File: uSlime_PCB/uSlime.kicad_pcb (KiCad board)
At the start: 2 copper layers, 25 x 22.6 mm, 43 parts, among them CN1 X1502WR-05K-N0SN, CN2 1.25T-2AW, J1 USB_C_Receptacle_USB2.0_14P, U1 ESP32-C6-MINI-1, U2 MSK-12C02_SMD_SPDT_SWITCH, U3 AP2112K-3.3TRG1, U4 MCP73831T-2ACI/OT, U5 BNO085

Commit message: v0.0.4a
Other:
- board text added: "v0.0.4a"
- board text removed: "v0.0.3a"
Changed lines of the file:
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@@
 		(tags "solder jumper open")
 		(property "Reference" "JP1"
-			(at 0 1.8 360)
+			(at 0 1.8 0)
 			(layer "B.SilkS")
 			(hide yes)
@@
 		)
 		(property "Value" "Jumper_3_Open"
-			(at 0 -1.9 360)
+			(at 0 -1.9 0)
 			(layer "B.Fab")
 			(effects
@@
 		)
 	)
-	(gr_text "v0.0.3a"
+	(gr_text "v0.0.4a"
 		(at 113.55 91.25 0)
 		(layer "B.SilkS")

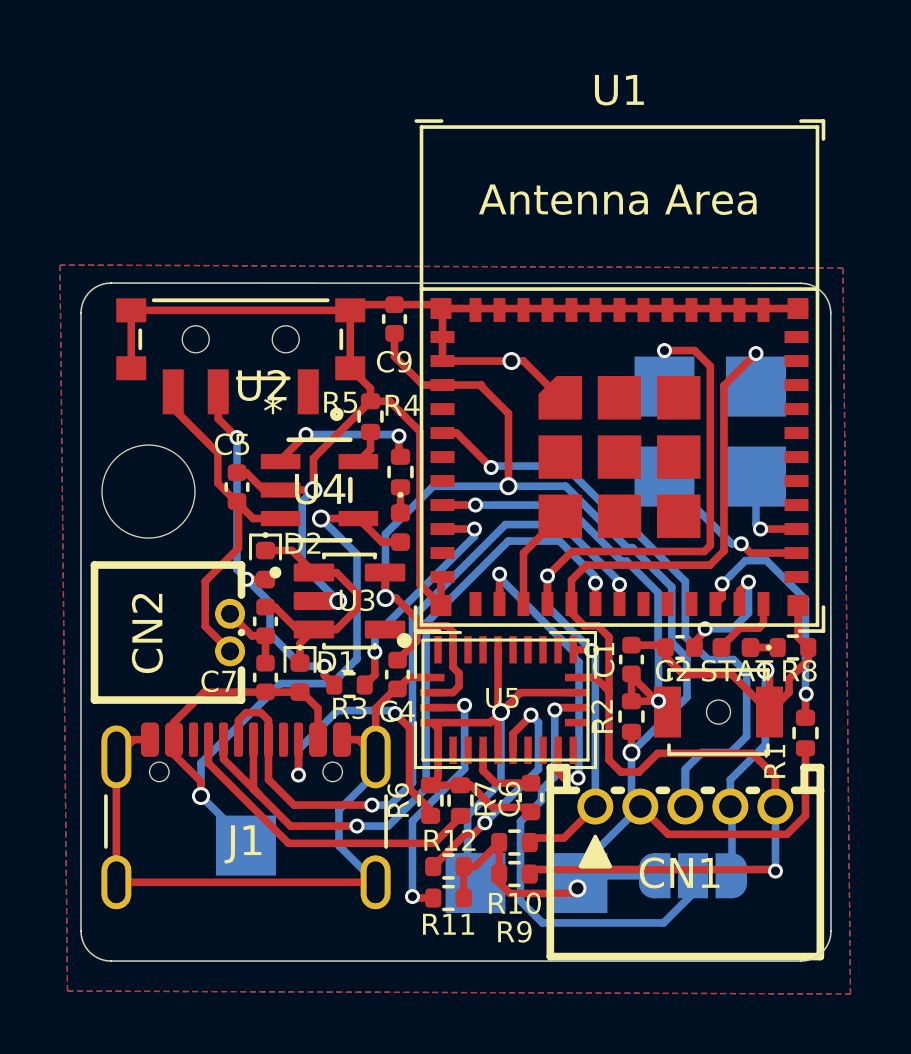
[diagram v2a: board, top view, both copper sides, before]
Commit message: v0.0.5: Invert CLKSEL pin to 3.3V
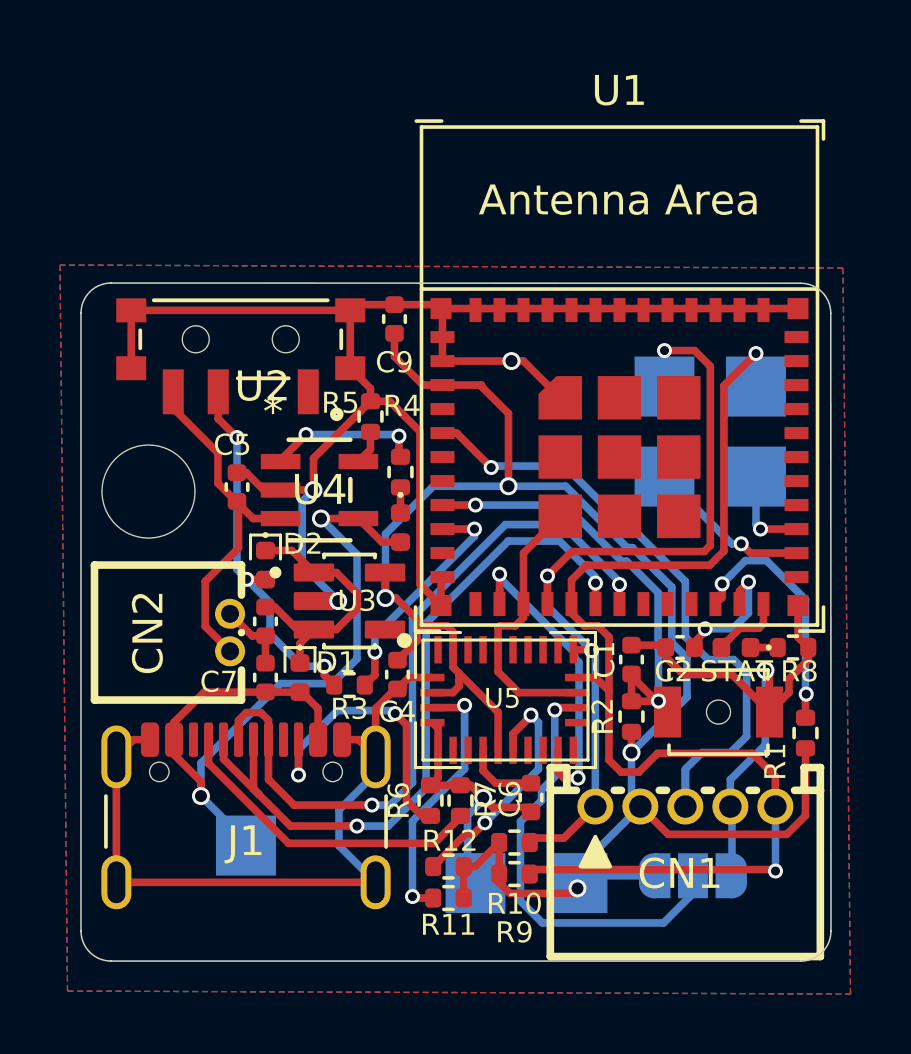
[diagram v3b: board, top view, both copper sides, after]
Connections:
- U5 pad 10: GND -> +3.3V
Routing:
- net GND: track 124.8 -> 118.8 mm
- net +3.3V: track 60.2 -> 63.3 mm
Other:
- board text added: "v0.0.5a"
- board text removed: "v0.0.4a"

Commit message: Connect pin 26 to GND
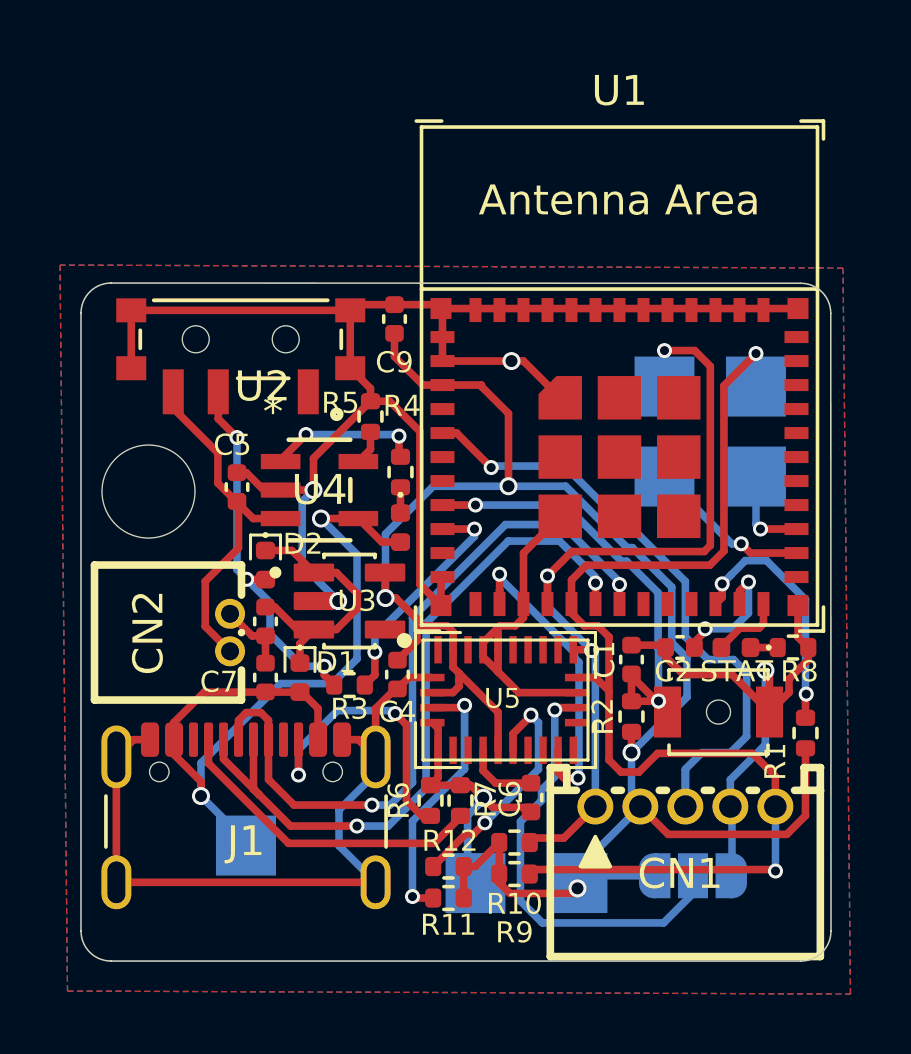
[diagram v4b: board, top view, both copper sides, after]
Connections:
- U5 pad 26: unconnected-(U5-XOUT32/CLKSEL1-Pad26) -> GND
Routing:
- net GND: track 118.8 -> 120.7 mm

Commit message: Add dingyifei to PCB ref
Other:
- board text added: "dingyifei"

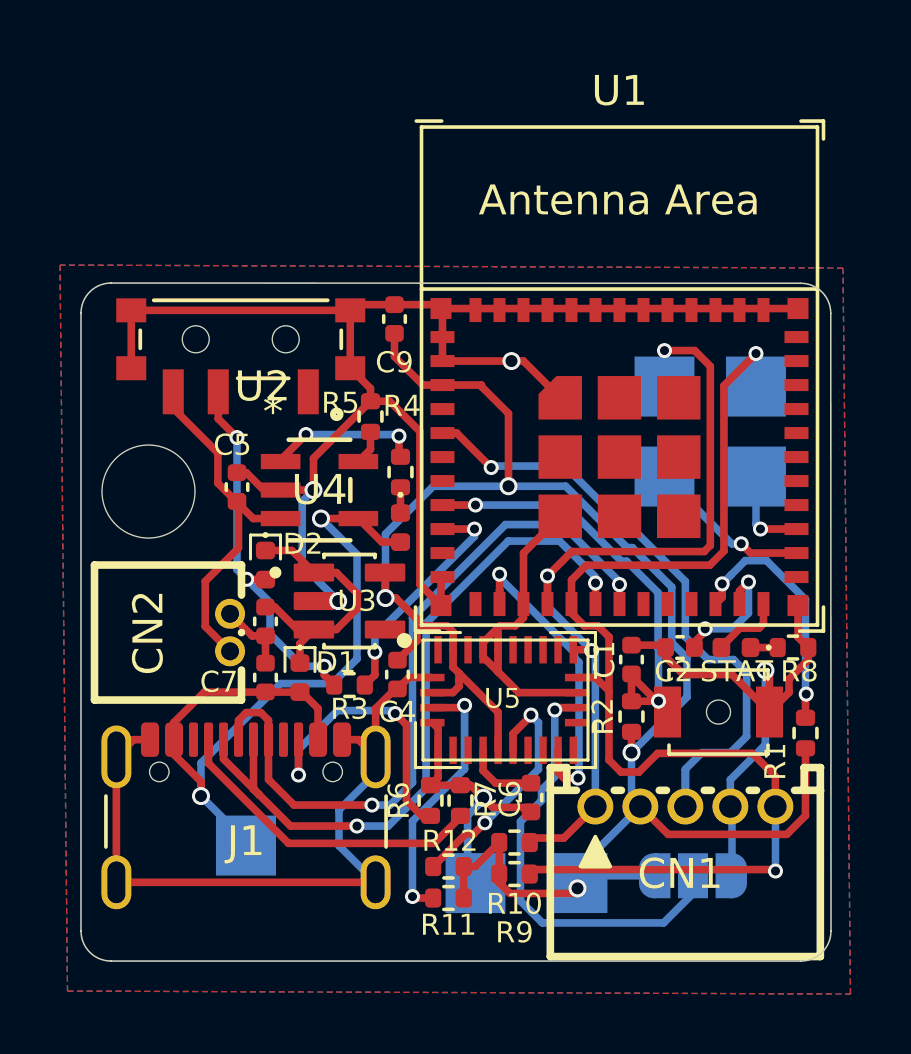
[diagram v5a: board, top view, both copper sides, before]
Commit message: Modify PCB to add resistors to pins 14, 15, 16
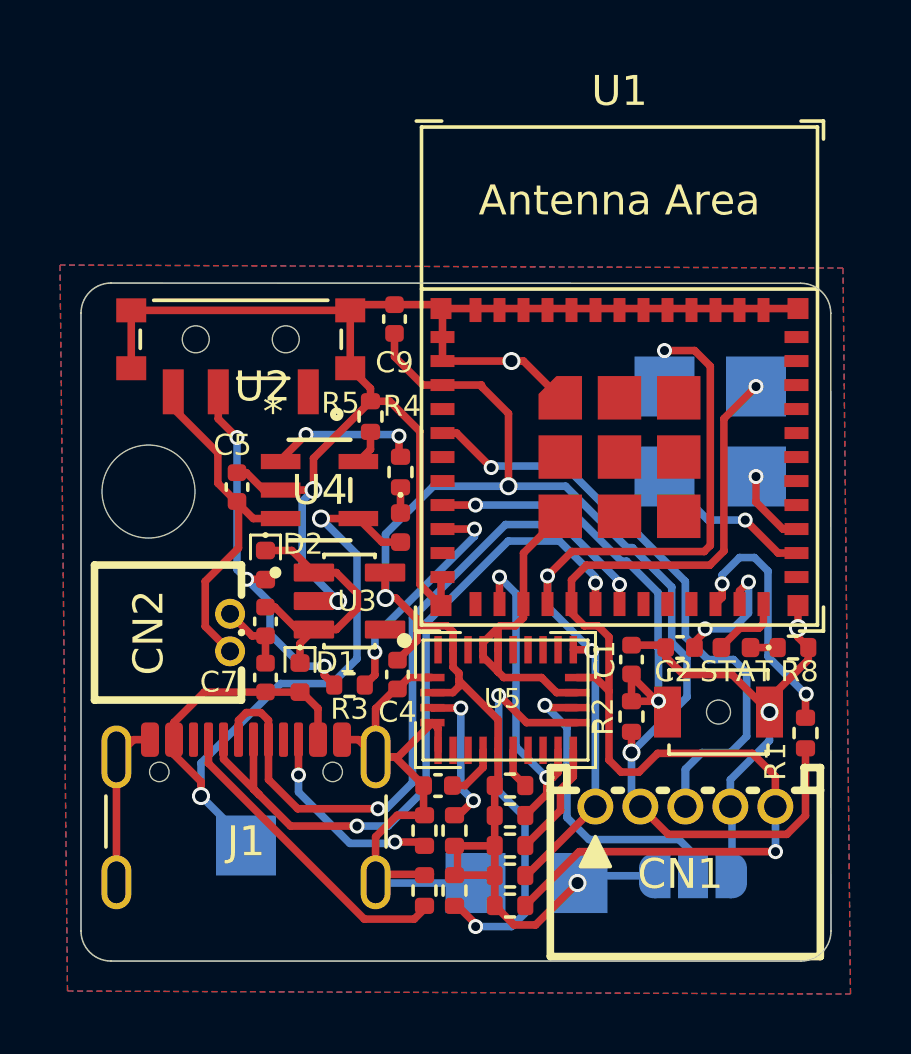
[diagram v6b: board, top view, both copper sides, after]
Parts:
- added R13: 10k, Resistor_SMD:R_0402_1005Metric, F.Cu at (115.0, 107.1)
- added R14: 10k, Resistor_SMD:R_0402_1005Metric, F.Cu at (115.0, 108.1)
- added R15: 10k, Resistor_SMD:R_0402_1005Metric, F.Cu at (113.1, 109.6)
- moved R12 3.39 mm to (115.0, 106.1), turned to 180 degrees
- moved R7 3.23 mm to (112.1, 109.6)
- moved C6 3.13 mm to (112.5, 106.1), turned to 0 degrees
- moved R11 2.26 mm to (113.1, 107.6), turned to 90 degrees
- moved R10 1.11 mm to (115.0, 109.1)
- moved R9 1.06 mm to (115.0, 110.1)
- moved R6 1.02 mm to (112.1, 107.6)
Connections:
- U5 pad 15: unconnected-(U5-ENV_SCL-Pad15) -> Net-(U5-ENV_SCL)
- U5 pad 16: unconnected-(U5-ENV_SDA-Pad16) -> Net-(U5-ENV_SDA)
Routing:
- net Net-(U5-ENV_SDA): track 0.00 -> 13.4 mm, vias 0 -> 2
- net GND: track 120.7 -> 110.1 mm
- net Net-(U5-NRST): track 8.18 -> 1.34 mm, vias 2 -> 0
- net Net-(JP1-C): track 14.7 -> 10.6 mm
- net Net-(U5-BOOTN): track 8.91 -> 4.95 mm
- net Net-(U5-ENV_SCL): track 0.00 -> 3.84 mm
- net Net-(J1-CC2): track 9.90 -> 6.83 mm
- net BNO_SCL: track 39.3 -> 37.3 mm
- net +3.3V: track 63.3 -> 65.0 mm
- net Net-(U5-CAP): track 2.47 -> 1.74 mm
- net BNO_SDA: track 27.3 -> 28.0 mm
- net BNO_INT: track 10.4 -> 11.0 mm

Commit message: v1.0.0 - Use 1206 LED, add resistor pack suggestion
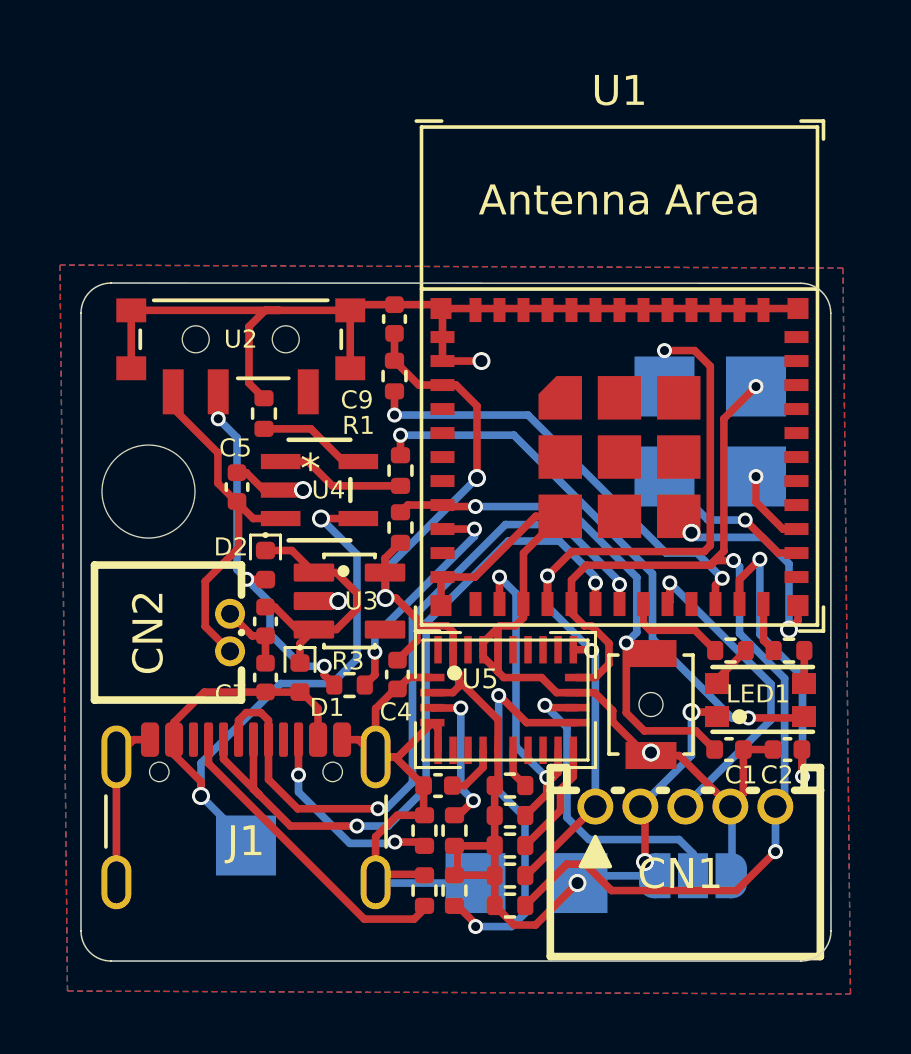
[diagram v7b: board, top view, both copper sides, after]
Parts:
- removed CHRG1, STAT1: LED, LED_SMD:LED_0402_1005Metric
- added LED1: MHT150RGBCT, uSlime-libs:LED-ARRAY-SMD_1206-4P-L3.2-W1.3-BR-EH, F.Cu at (123.3, 103.2)
- added R16: 1k, Resistor_SMD:R_0402_1005Metric, F.Cu at (122.3, 101.6)
- ?: value (none) -> 3mm_THT_Hole; footprint (none) -> uSlime-libs:3mm_THT_Hole
- R5: value 2k -> 2.2k
- moved R1 18.1 mm to (111.1, 92.5), turned to 90 degrees
- moved R2 9.95 mm to (111.3, 97.5)
- moved C2 4.94 mm to (124.2, 104.9)
- moved C1 4.42 mm to (122.2, 104.9), turned to 0 degrees
- moved R5 3.55 mm to (106.8, 93.7)
- moved RESET1 2.26 mm to (119.7, 103.4), turned to 90 degrees
- moved R8 0.17 mm to (124.2, 101.6), turned to 0 degrees
- moved R4 0.05 mm to (111.3, 95.6)
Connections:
- R4 pad 1: Net-(CHRG1-K) -> STAT
- R4 pad 2: Net-(U4-STAT) -> Net-(LED1---Pad4)
- R8 pad 1: GND -> /ESP32-C6FH4/IO18/~{CS}
- U1 pad 20: /ESP32-C6FH4/IO15/LP -> BNO_INT2
- U1 pad 5: BNO_INT2 -> /ESP32-C6FH4/IO2
- U4 pad 1: Net-(U4-STAT) -> STAT
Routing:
- net Net-(LED1---Pad4): track 0.00 -> 19.3 mm, vias 0 -> 2
- net +3.3V: track 65.0 -> 46.4 mm, vias 4 -> 5
- net BNO_INT2: track 21.6 -> 10.8 mm
- net GND: track 110.1 -> 100.7 mm, vias 5 -> 6
- net /ESP32-C6FH4/IO8: track 8.45 -> 14.9 mm
- net /ESP32-C6FH4/IO9/BOOT: track 4.47 -> 10.5 mm
- net Net-(U4-STAT): track 5.08 -> 0.00 mm, vias 2 -> 0
- net STAT: track 0.00 -> 4.33 mm
- net /ESP32-C6FH4/IO14: track 0.00 -> 3.52 mm
- net Net-(U4-PROG): track 1.16 -> 3.60 mm
- net /ESP32-C6FH4/ESP_EN: track 16.0 -> 18.2 mm
- net VBUS: track 27.5 -> 25.7 mm
- net Net-(LED1---Pad2): track 0.00 -> 1.35 mm
- net Net-(CHRG1-K): track 0.86 -> 0.00 mm
- net /ESP32-C6FH4/IO18/~{CS}: track 2.40 -> 1.69 mm
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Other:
- board text added: "v1.0.0"
- board text removed: "CHRG"
- board text removed: "RST"
- board text removed: "STAT"
- board text removed: "v0.0.5a"

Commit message: Remove GPIO9 capacitor causing boot problems
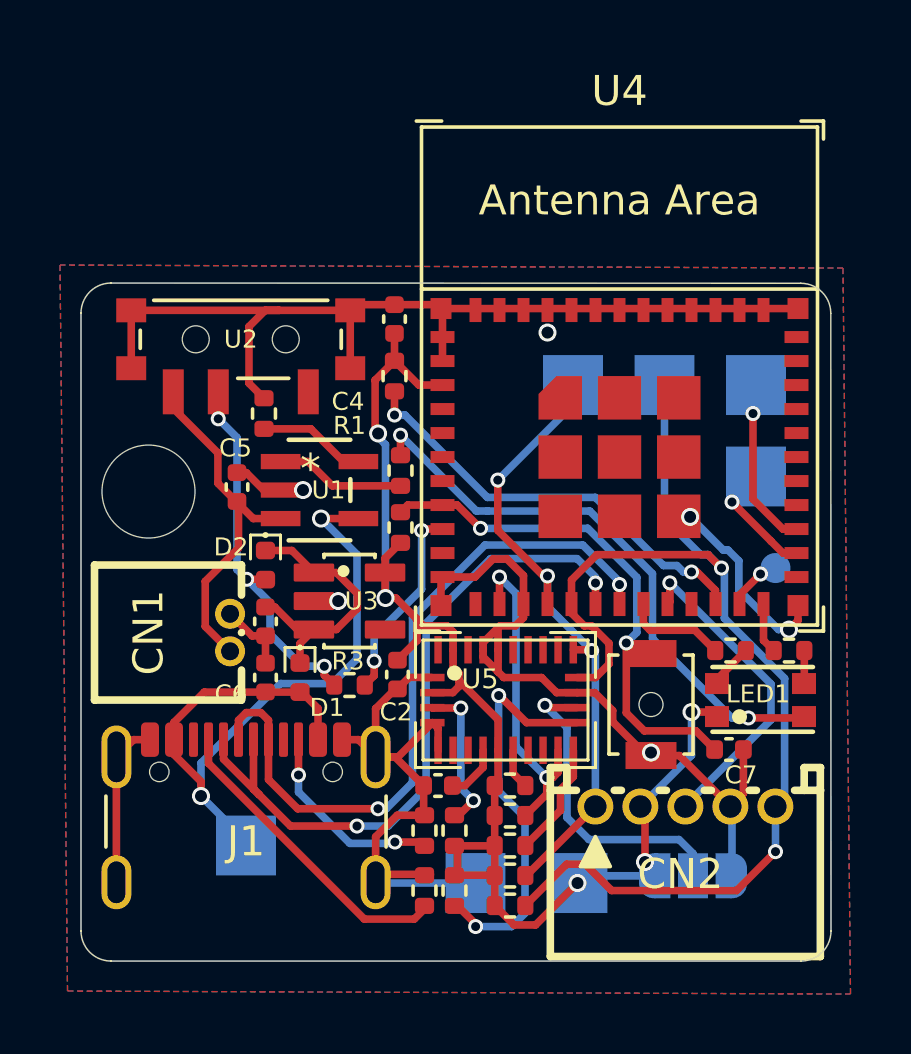
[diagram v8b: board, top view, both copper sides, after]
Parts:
- removed the C2 at (124.2, 104.9)
- added TP1: BOOT, TestPoint:TestPoint_Pad_D1.0mm, B.Cu at (123.8, 98.8)
- C2: renamed from C4; value 10uF -> 0.1uF
- C4: renamed from C9; value 0.1uF -> 10uF
- moved TP4 3.05 mm to (120.1, 92.8)
- moved TP6 3.05 mm to (117.0, 92.8)
- moved TP3 3.05 mm to (123.2, 95.8)
- moved TP5 3.05 mm to (123.2, 92.8)
- moved G*** 0.10 mm to (115.0, 100.2)
- renumbered C6 to C1, C7 to C6, C1 to C7, CN2 to CN1, CN1 to CN2, R9 to R10, R10 to R11, R8 to R12, R12 to R13, R13 to R14, R14 to R15, R5 to R2, R6 to R4, R11 to R5, R2 to R6, R15 to R7, R7 to R8, R4 to R9, TP5 to TP2, TP2 to TP4, TP4 to TP5, TP1 to TP6, TP6 to TP7, TP7 to TP8, U4 to U1, U1 to U4
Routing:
- net /ESP32-C6FH4/IO9/BOOT: track 10.5 -> 1.87 mm, vias 2 -> 1
- net GND: track 100.7 -> 93.9 mm
- net BNO_SDA: track 28.0 -> 21.4 mm
- net /ESP32-C6FH4/IO21/POCI: track 2.58 -> 5.71 mm
- net /ESP32-C6FH4/IO20/PICO: track 5.46 -> 4.04 mm
- net BatSense: track 7.83 -> 6.65 mm
- net +3.3V: track 46.4 -> 45.7 mm
- net D+ P: track 24.6 -> 24.0 mm
- net /ESP32-C6FH4/IO8: track 14.9 -> 14.4 mm
- net BNO_SCL: track 37.3 -> 37.5 mm, vias 3 -> 2
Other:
- board text added: "BOOT"
